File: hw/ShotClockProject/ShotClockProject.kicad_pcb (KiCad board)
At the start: 2 copper layers, 117 parts, among them IC1 TP4056-42-ESOP8_Rearanged, J1 USB4120-03-C_REVA, J10 DW254W-22-20-85, J2 Conn_ST_STDC14, J3 Conn_01x06_Pin, J4 SM03B-SRSS-TB(LF)(SN)(P), J5 Conn_01x02_Pin, J6 Conn_01x03_Pin, J7 DW254W-22-20-85, J8 DW254W-22-20-85, J9 DW254W-22-20-85, Q1 Q_NPN_BCE, Q2 Q_PMOS_SGD, Q3 Q_NPN_BCE, Q4 Q_NPN_BCE, SW1 PS-5824SVB-6PL, SW2 SW_SPDT, SW3 SW_SPST, SW4 SW_SPST, SW5 SW_SPST, U1 STM32F103RCT6, U2 LD39015M33R, U3 TPS63000, U4 TPS63000, U5 M74HC14YRM13TR, Y1 16MHz

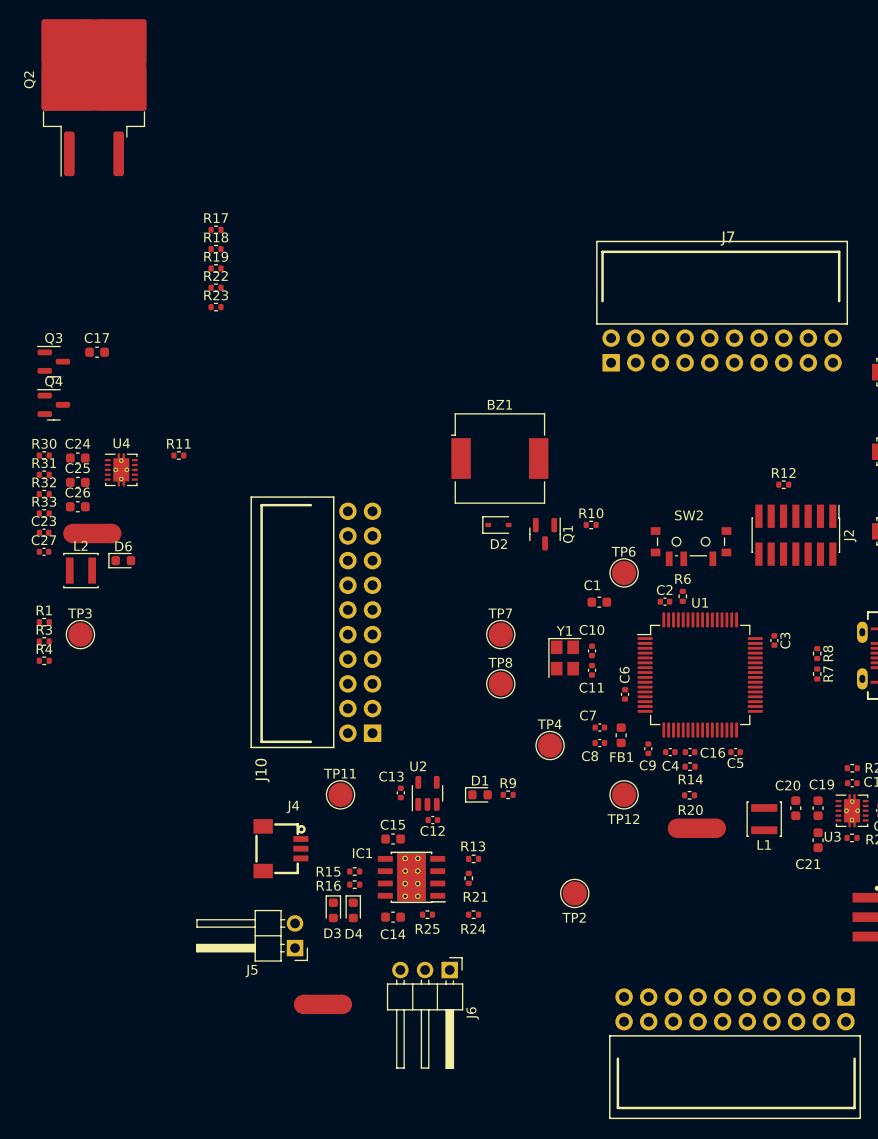
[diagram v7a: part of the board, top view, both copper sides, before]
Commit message: Updated Layout
Placed 5V regulator
Placed new shutoff circuit when charging
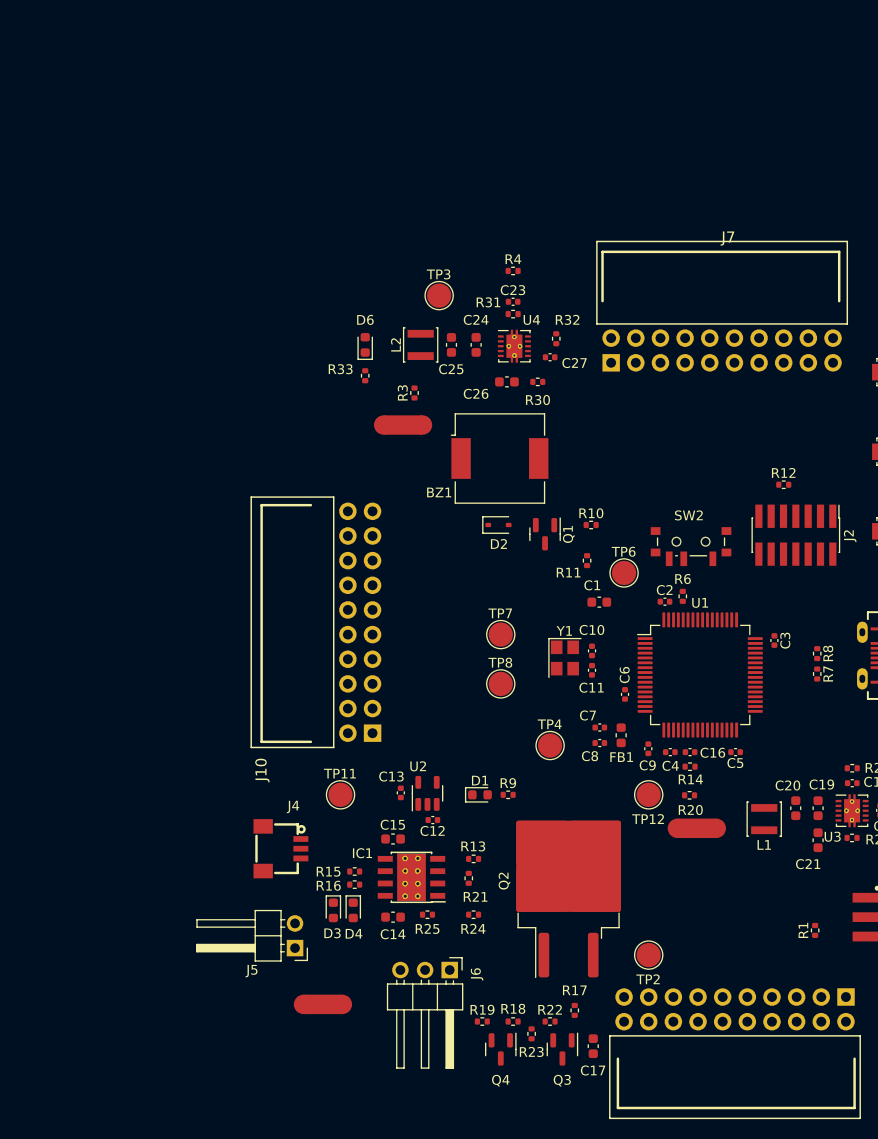
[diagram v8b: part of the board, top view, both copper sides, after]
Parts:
- moved Q2 95.9 mm to (134.0, 116.8)
- moved R17 88.5 mm to (134.6, 130.2), turned to 90 degrees
- moved Q3 88.1 mm to (133.3, 134.2), turned to -90 degrees
- moved C17 87.9 mm to (136.5, 133.8), turned to -90 degrees
- moved R1 85.5 mm to (159.4, 121.9), turned to 90 degrees
- moved R18 85.3 mm to (128.3, 131.3), turned to 180 degrees
- moved R22 83.1 mm to (132.1, 131.3)
- moved R19 82.3 mm to (125.1, 131.3)
- moved R23 81.6 mm to (130.2, 132.6), turned to -90 degrees
- moved Q4 80.8 mm to (127.0, 134.2), turned to -90 degrees
- moved R4 62.8 mm to (128.3, 54.0)
- moved C27 55.9 mm to (132.1, 62.9)
- moved R32 55.1 mm to (132.7, 61.0), turned to -90 degrees
- moved C23 53.9 mm to (128.3, 57.1)
- moved R30 51.4 mm to (130.8, 65.4)
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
